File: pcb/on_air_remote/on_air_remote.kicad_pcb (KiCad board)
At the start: 2 copper layers, 36.5 x 71 mm, 19 parts, among them J1 USB_B_Micro, Q1 IRLL014NPBF, SW1 TX, U1 CH340G, U2 NRF24L01_Breakout, Y1 12MHz

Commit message: Update on_air_remote.kicad_pcb
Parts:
- moved R7 63.8 mm to (131.0, 142.0), turned to 270 degrees
- moved R6 61.1 mm to (133.5, 142.0), turned to 270 degrees
- moved R4 54.3 mm to (138.5, 142.0), turned to 270 degrees
- moved R3 48.6 mm to (130.0, 137.0), turned to 180 degrees
- moved R1 41.4 mm to (144.0, 109.5), turned to 90 degrees
- moved R2 39.7 mm to (130.0, 134.5)
- moved Q1 30.5 mm to (149.0, 109.5), turned to 90 degrees
- moved R5 21.2 mm to (136.0, 142.0), turned to 270 degrees
- moved C4 13.0 mm to (152.0, 154.0), turned to 270 degrees
- moved C3 10.6 mm to (144.5, 143.0)
- moved C2 5.50 mm to (122.5, 155.0)
- moved C1 5.46 mm to (126.5, 155.0)
- moved Y1 5.00 mm to (127.0, 152.5), turned to 180 degrees
- moved U1 1.50 mm to (145.5, 152.5), turned to 270 degrees
- turned SW1 to 270 degrees
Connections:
- A1 pad 23: Net-(A1-Pad23) -> /SHUTDOWN
- A1 pad 7: /SHUTDOWN -> Net-(A1-Pad7)
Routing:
- net +3V0: track 0.00 -> 81.8 mm
- net /CE: track 0.00 -> 74.2 mm
- net /~CSN: track 0.00 -> 52.7 mm
- net /MOSI: track 0.00 -> 47.7 mm
- net /MISO: track 0.00 -> 41.9 mm
- net /Vbatt: track 0.00 -> 40.1 mm
- net /SCK: track 0.00 -> 40.0 mm
- net Net-(C2-Pad1): track 0.00 -> 22.7 mm
- net Net-(C1-Pad1): track 0.00 -> 19.6 mm
- net /SHUTDOWN: track 0.00 -> 19.3 mm
- net GND: track 0.00 -> 14.5 mm
- net /~DTR: track 0.00 -> 12.9 mm
- net /TXD: track 0.00 -> 12.3 mm
- net Net-(J1-Pad3): track 0.00 -> 11.9 mm
- net Net-(J1-Pad2): track 0.00 -> 11.3 mm
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- added copper zone on B.Cu, net GND
- added copper zone on F.Cu, net GND
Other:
- board size 36.5 x 71 mm -> 36.5 x 72.5 mm

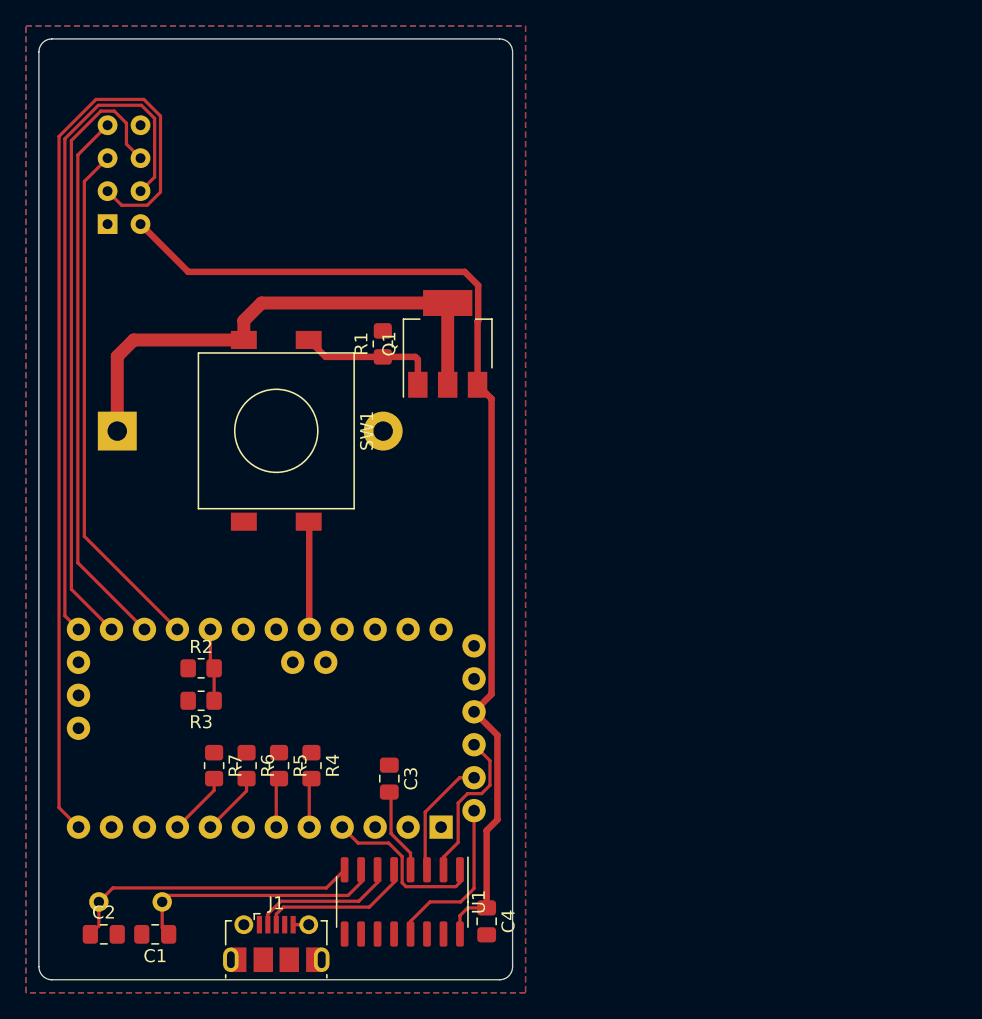
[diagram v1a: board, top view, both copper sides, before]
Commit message: single sided pcb done, ready for mill
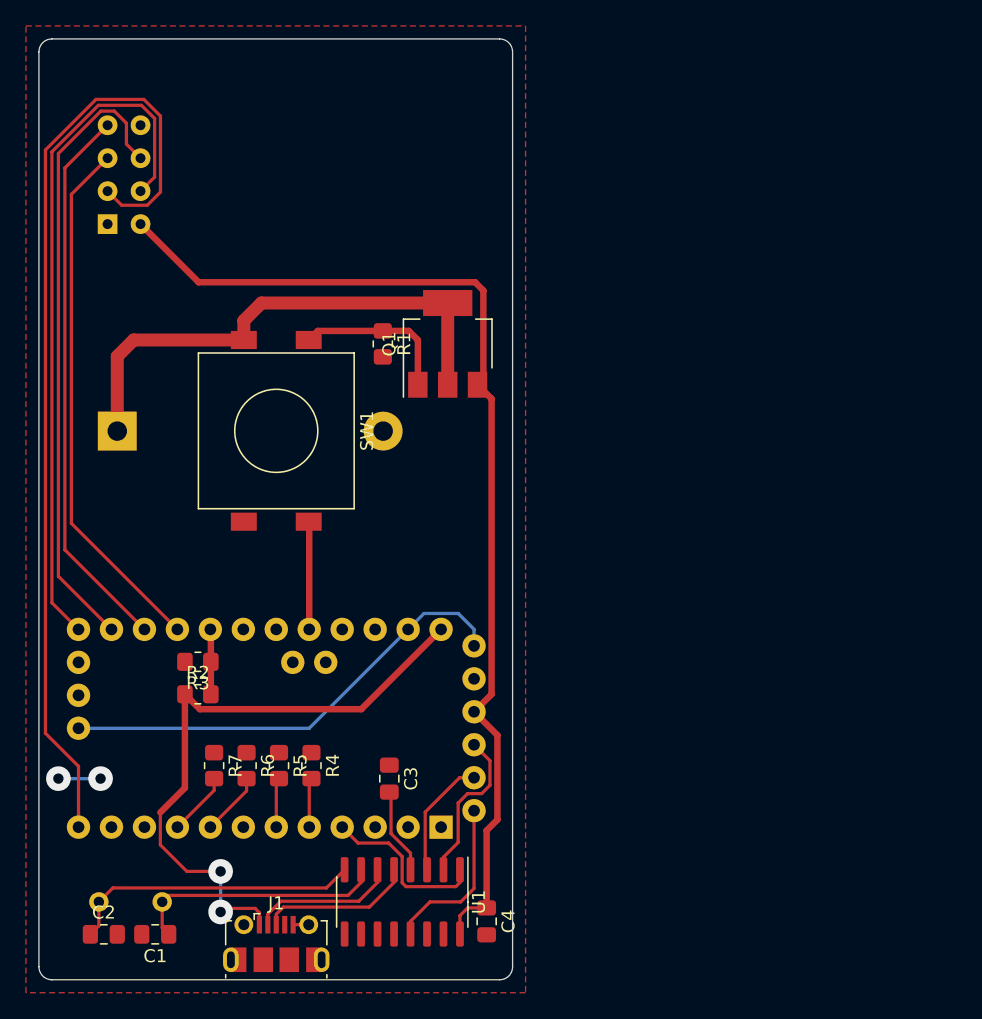
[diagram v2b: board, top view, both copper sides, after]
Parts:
- moved R3 3.01 mm to (129.8, 134.0)
- moved R2 2.02 mm to (129.8, 136.5)
- turned R1 to 270 degrees
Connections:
- A1 pad 24: +3V0 -> (no net)
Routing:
- net +5V: track 0.00 -> 47.9 mm, vias 0 -> 2
- net GND: track 14.5 -> 53.6 mm, vias 0 -> 2
- net /SHUTDOWN: track 19.3 -> 20.8 mm
- net /CE: track 74.2 -> 75.1 mm
- net /MISO: track 41.9 -> 42.8 mm
- net /~CSN: track 52.7 -> 53.5 mm
- net /SCK: track 40.0 -> 40.8 mm
- net /MOSI: track 47.7 -> 48.5 mm
- removed copper zone on B.Cu, net GND
